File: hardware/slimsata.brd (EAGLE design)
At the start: 20.3 x 54.6 mm, 2 parts, among them CON1 MOLEX_67492, CON2 MOLEX_47300

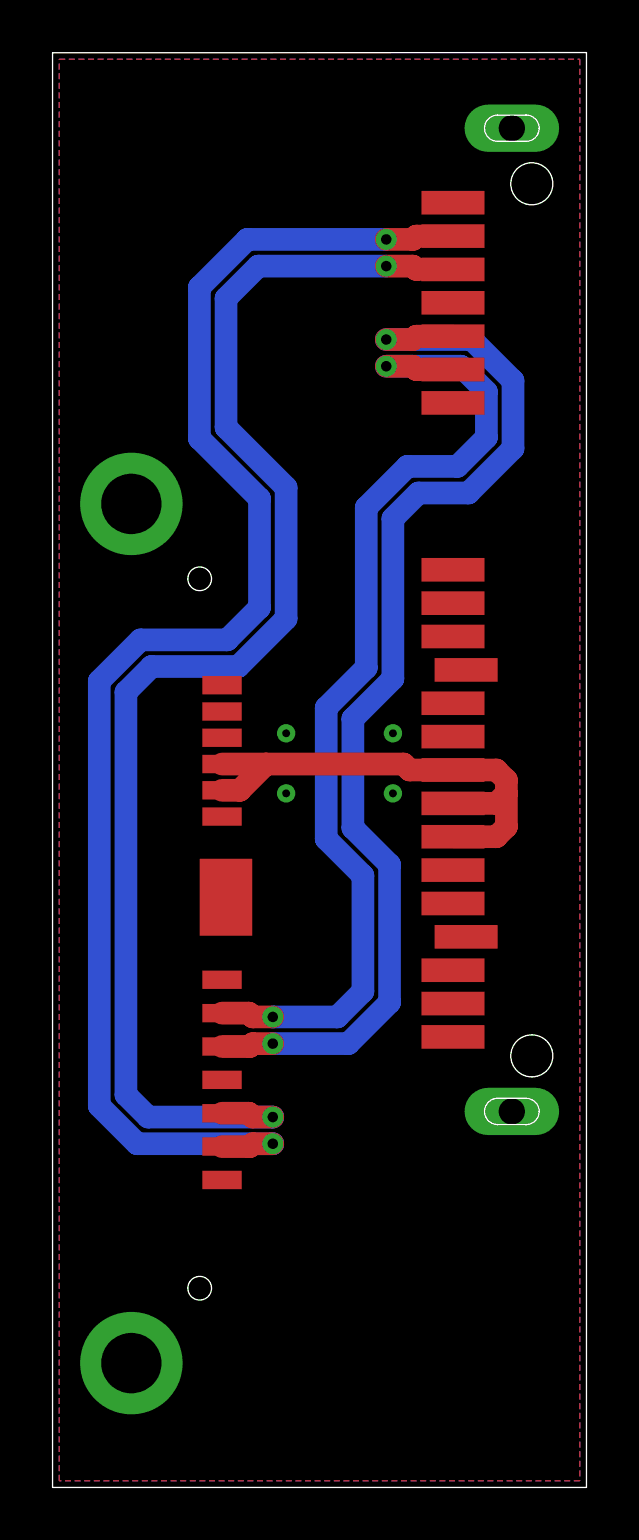
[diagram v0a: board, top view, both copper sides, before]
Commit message: Längenausgleich auf 0.4 mil
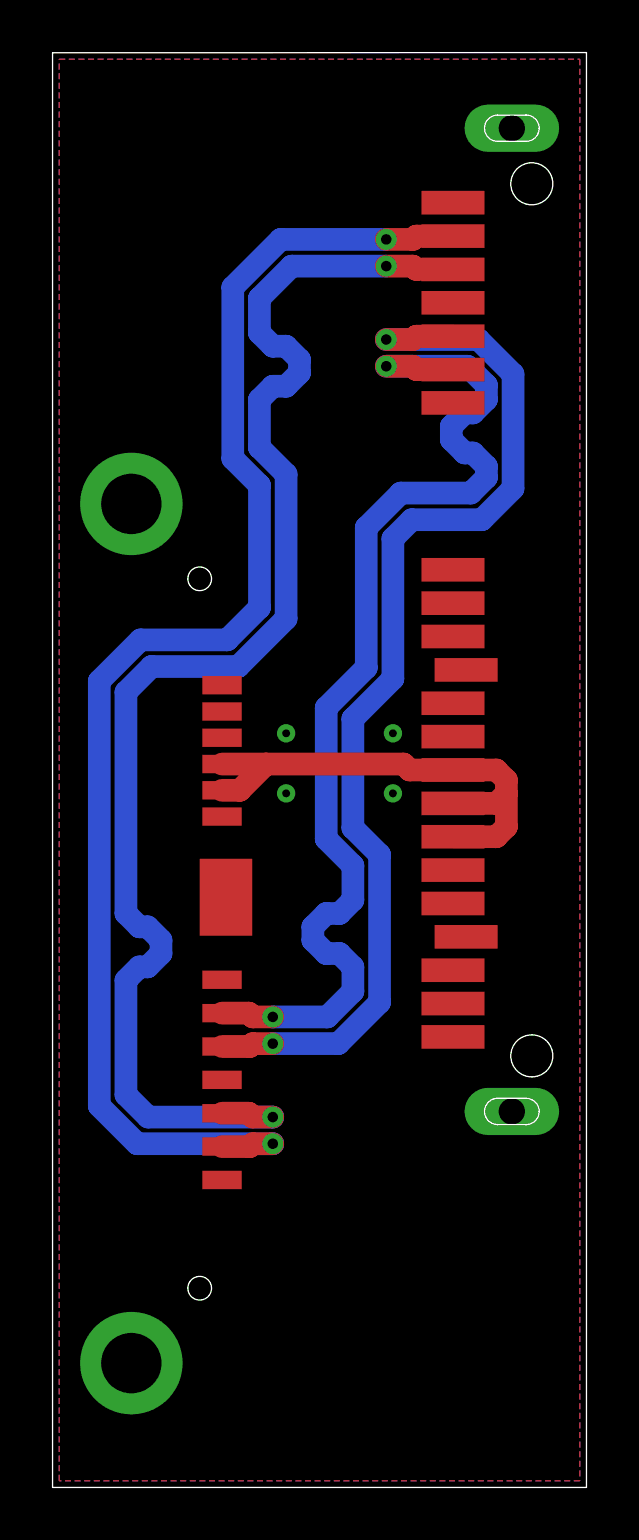
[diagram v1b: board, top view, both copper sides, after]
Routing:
- net B_P: track 39.7 -> 43.1 mm
- net A_P: track 56.2 -> 54.4 mm
- net A_N: track 52.9 -> 54.4 mm

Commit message: Package des Molex 447300 von -1005 zu 1020 geändert
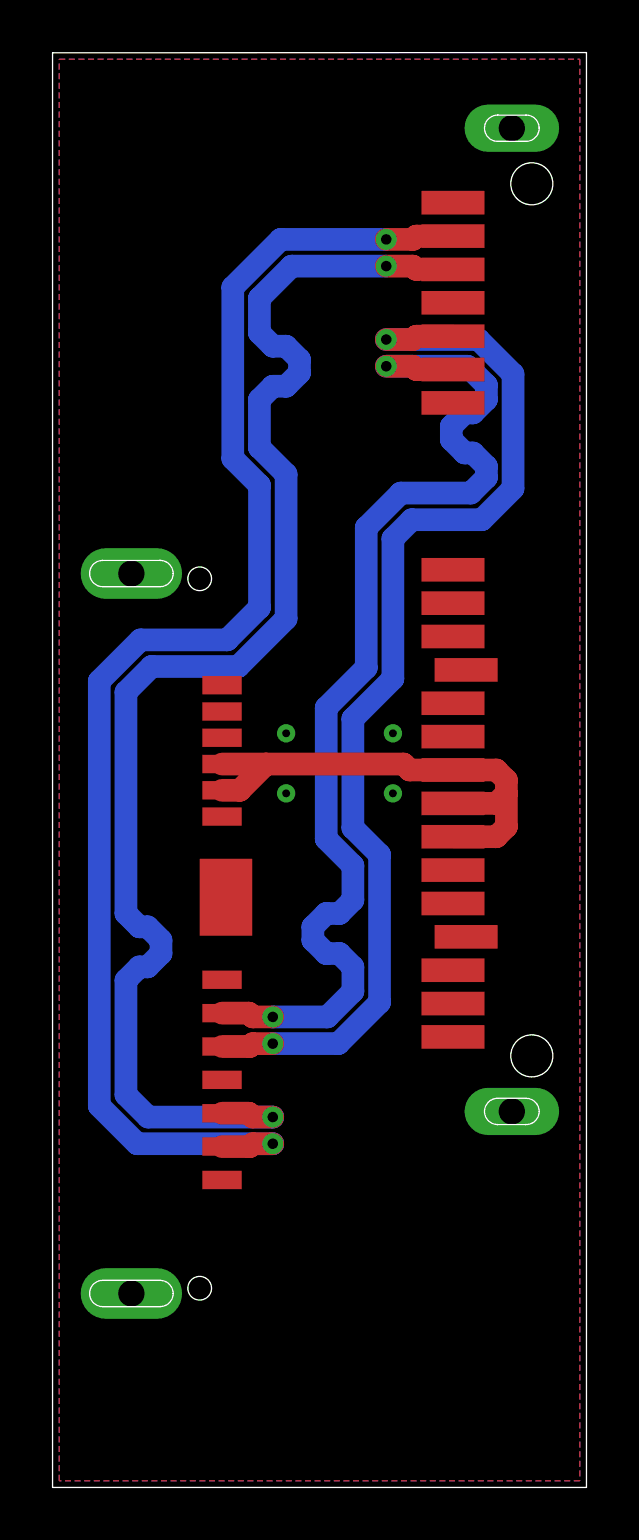
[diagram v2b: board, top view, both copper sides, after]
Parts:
- CON2: device sata:MOLEX_47300-100X/101X -> sata:MOLEX_47300-102X/103X
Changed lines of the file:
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@@
 <elements>
 <element name="CON1" library="sata" package="MOLEX_67492" value="MOLEX_67492" x="20.32" y="33.02" rot="R90"/>
-<element name="CON2" library="sata" package="MOLEX_47300-100X/101X" value="MOLEX_47300" x="0" y="21.082" rot="R270"/>
+<element name="CON2" library="sata" package="MOLEX_47300-102X/103X" value="MOLEX_47300" x="0" y="21.082" rot="R270"/>
 </elements>
 <signals>
@@
 </signal>
 </signals>
-<errors>
-</errors>
 </board>
 </drawing>

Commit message: Molex 47300 durch Kombivariante ersetzt
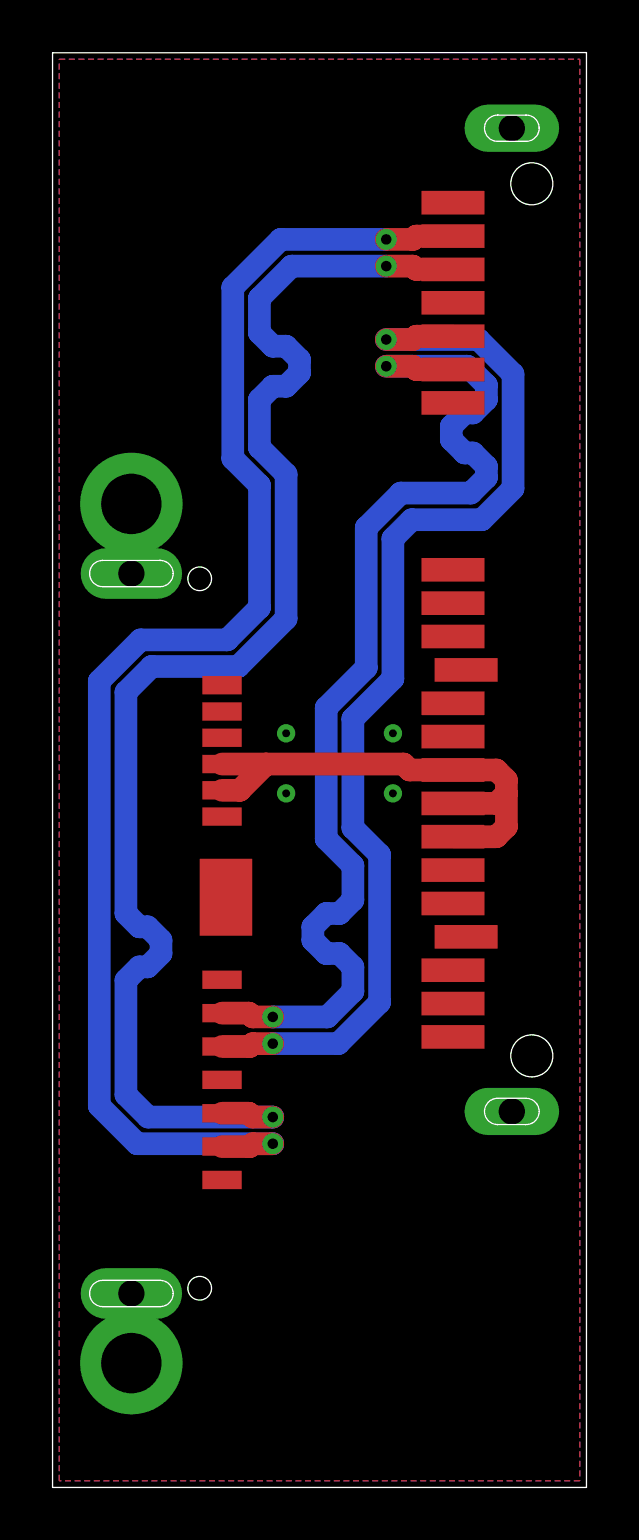
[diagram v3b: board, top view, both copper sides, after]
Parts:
- CON2: device sata:MOLEX_47300-102X/103X -> sata:MOLEX_47300-100X/101X/102X/103X
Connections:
- net GND: now also CON2.MECH4, CON2.MECH5
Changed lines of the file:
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@@
 <elements>
 <element name="CON1" library="sata" package="MOLEX_67492" value="MOLEX_67492" x="20.32" y="33.02" rot="R90"/>
-<element name="CON2" library="sata" package="MOLEX_47300-102X/103X" value="MOLEX_47300" x="0" y="21.082" rot="R270"/>
+<element name="CON2" library="sata" package="MOLEX_47300-100X/101X/102X/103X" value="MOLEX_47300" x="0" y="21.082" rot="R270"/>
 </elements>
 <signals>
@@
 <contactref element="CON1" pad="MECH2"/>
 <contactref element="CON1" pad="MECH1"/>
+<contactref element="CON2" pad="MECH4"/>
 <contactref element="CON2" pad="MECH3"/>
 <contactref element="CON2" pad="MECH2"/>
-<contactref element="CON2" pad="MECH1"/>
 <contactref element="CON1" pad="P4"/>
 <contactref element="CON1" pad="P5"/>
@@
 <via x="12.954" y="28.702" extent="1-16" drill="0.3"/>
 <via x="12.954" y="26.416" extent="1-16" drill="0.3"/>
+<contactref element="CON2" pad="MECH1"/>
+<contactref element="CON2" pad="MECH5"/>
 </signal>
 </signals>
